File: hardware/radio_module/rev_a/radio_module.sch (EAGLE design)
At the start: 121 parts, among them J1 MODULE_GENERIC, J2 TC2030-JLINK-NL, J4 NANO_SIM, J5 TC2030-JLINK-L, P1 MOLEX_73251-135X, P2 MOLEX_73251-135X, Q1 MOSFET-NCHANNELXFDN-3, Q2 MOSFET-NCHANNELXFDN-3, Q3 MOSFET-NCHANNELXFDN-3, Q4 MOSFET-NCHANNELXFDN-3, Q5 NX3008PBK, Q6 NX3008PBK, Q7 NX3008PBK, U1 NUCLEUM, U10 TXB0106, U11 SAM4LC8BA, U12 UBLOX_SARA_G350, U2 TLV62130, U4 LTC2941, U5 LTC2941, U6 IM880_MODULE, U7 PCA9544AQFN-N20, U8 TLV62130, U9 LTC2941, X2 16 MHz

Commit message: used pats tool. worked well
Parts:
- removed C28, C32: 10uF, passives:CAPACITOR0402_CAP
- removed C30, C34: 3.3nF, passives:CAPACITOR0402_CAP
- removed C31, C35: 22uF, passives:CAPACITOR0402_CAP
- added C11: 10nF, passives:CAPACITOR0402_CAP
- added C14, C15, C16, C17, C18: 100nF, passives:CAPACITOR0402_CAP
- C1, C2: value 47pF -> 8pF; DIGIKEY (none) -> 490-8230-1-ND
- C10: value 56pF -> 3.3nF
- C19: value 1uF -> 100nF; DIGIKEY (none) -> 490-10777-1-ND
- C20: value 8 pF -> 100nF; DIGIKEY 490-8230-1-ND -> (none)
- C21: value 8 pF -> 1uF; DIGIKEY 490-8230-1-ND -> (none)
- C22: value 100 nF -> 4.7uF; DIGIKEY 490-10777-1-ND -> 490-13252-1-ND
- C23, C24: value 100 nF -> 10uF; DIGIKEY 490-10777-1-ND -> (none)
- C25, C26: value 100 nF -> 22uF; DIGIKEY 490-10777-1-ND -> (none)
- C27: value 4.7 uF -> 220uF; device passives:CAPACITOR0402_CAP -> passives:CAPACITOR1210_CAP; DIGIKEY 490-13252-1-ND -> (none)
- C3: value 47pF -> 33pF; device passives:CAPACITOR0402_CAP -> passives:CAPACITOR0603_CAP
- C5: value 33pF -> 47pF; device passives:CAPACITOR0603_CAP -> passives:CAPACITOR0402_CAP
- C6: value 100nF -> 47pF
- C7: value 220uF -> 47pF; device passives:CAPACITOR1210_CAP -> passives:CAPACITOR0402_CAP
- C8: value 100nF -> 56pF
- C9: value 10nF -> 3.3nF
- FB4: value 1.5 k -> 1.5k
- L6: value 22 uH -> 22uH
- R1: value 10K -> 0
- R10: value 1k -> 10k
- R11, R12: value 0 -> 10k; DIGIKEY (none) -> 1276-3431-1-ND
- R13: value 750k -> 10k; DIGIKEY (none) -> 1276-3431-1-ND
- R14: value 240k -> 10k; DIGIKEY (none) -> 1276-3431-1-ND
- R15, R21: value 100K -> 10k
- R16, R17: value 100 k -> 10k; DIGIKEY 1276-3432-1-ND -> (none)
- R18: value 10 k -> 10k; DIGIKEY 1276-3431-1-ND -> (none)
- R19: value 750k -> 10k
- R2: value 1k -> 0
- R20: value 200k -> 10k
- R24: DIGIKEY (none) -> 1276-3431-1-ND
- R25: value 0.423 -> 100k
- R26, R27: value 10k -> 100k; DIGIKEY (none) -> 1276-3432-1-ND
- R28, R30, R31, R32: value 10k -> 100k
- R29: value 0.016 -> 100k
- R3: value 100k -> 0; DIGIKEY (none) -> 1276-3431-1-ND
- R33: value 10k -> 100k; DIGIKEY 1276-3431-1-ND -> (none)
- R38: value 100k -> 200k
- R39: value 100k -> 240k
- R4: value 10k -> 0
- R40, R41: value 100k -> 750k
- R5: value 0 -> 0.016; DIGIKEY 1276-3431-1-ND -> (none)
- R6: value 0 -> 0.423; DIGIKEY 1276-3431-1-ND -> (none)
- R7: value 10k -> 3.333; DIGIKEY 1276-3431-1-ND -> (none)
- R8: value 10k -> 1k; DIGIKEY 1276-3431-1-ND -> (none)
- R9: value 3.333 -> 1k
- renumbered C29 to C12, C33 to C13
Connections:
- net 3V3: now also C16.1, C17.1, C18.1, C25.2, R11.2, R12.1, R13.1, R14.1, R19.2, R20.2, R24.1, R40.2, R6.2, R7.2; no longer C23.1, C24.1, C25.1, C31.2, R13.2, R22.2, R23.2, R24.2, R25.2, R33.1, R4.1, R7.1, R8.1, R9.2
- net 3V8: now also C26.2, R22.2, R23.2, R41.2, R5.2; no longer C35.2, R19.2, R30.2, R31.2, R32.2
- net 5V: now also C23.1, C24.1; no longer C28.1, C32.1
- net CONTROLLER_BUCK/LDO_N: now also R11.1; no longer R18.1
- net CONTROLLER_SWDCLK: now also R27.1; no longer R17.1
- net CONTROLLER_SWDIO: now also R26.1; no longer R16.1
- net CONTROLLER_XIN: now also C1.1; no longer C20.1
- net CONTROLLER_XOUT: now also C2.1; no longer C21.1
- net GND: now also C10.1, C11.2, C14.2, C15.2, C16.2, C17.2, C18.2, C25.1, C26.1, C5.2, C9.1, R30.1, R31.1, R32.1, R37.1, R38.1; no longer C10.2, C25.2, C26.2, C28.2, C3.2, C30.1, C31.1, C32.2, C34.1, C35.1, C9.2, R14.1, R20.1, R34.1, R36.1, R41.1
- net GSM_3V8: now also R33.2, R5.1, R8.2; no longer R2.2, R29.1, R37.2
- net GSM_GATED: now also C11.1, C14.1, C27.1; no longer C10.1, C7.1, C9.1
- net GSM_GAUGE_ALERT: now also R21.1; no longer R30.1
- net GSM_GAUGE_SCL: now also R22.1; no longer R31.1
- net GSM_GAUGE_SDA: now also R23.1; no longer R32.1
- net GSM_LED: now also R31.2; no longer R35.2
- net GSM_POWER_GATE: now also R32.2, R33.1; no longer R36.2, R37.1
- net IM880_3V3: now also R36.2, R6.1, R9.2; no longer R10.2, R25.1, R40.2
- net IM880_GATED: now also C21.1; no longer C19.1
- net IM880_GAUGE_ALERT: now also R18.1; no longer R26.1
- net IM880_GAUGE_SCL: now also R19.1; no longer R27.1
- net IM880_GAUGE_SDA: now also R20.1; no longer R28.1
- net IM880_NETWORK: now also R30.2; no longer R34.2
- net IM880_POWER_GATE: now also R36.1, R37.2; no longer R40.1, R41.2
- net N$1: now also C7.1; no longer C4.1
- net N$12: now also R24.2; no longer R33.2
- net N$15: now also C20.1, R25.2; no longer C6.1, R3.2
- net N$16: now also R25.1; no longer R3.1
- net N$17: now also R3.1; no longer R5.1
- net N$18: now also R4.1; no longer R6.1
- net N$2: now also C6.1; no longer C3.1
- net N$25: now also R1.1; no longer R11.1
- net N$26: now also R2.1; no longer R12.1
- net N$27: now also R9.1; no longer R10.1
- net N$3: now also C5.1; no longer C2.1
- net N$33: now also C15.1; no longer C22.1
- net N$34: now also C9.2; no longer C30.2
- net N$36: now also R28.1; no longer R15.1
- net N$37: now also R39.2, R40.1; no longer R13.1, R14.2
- net N$38: now also C10.2; no longer C34.2
- net N$4: now also C4.1; no longer C1.1
- net N$40: now also R29.1; no longer R21.1
- net N$41: now also R38.2, R41.1; no longer R19.1, R20.2
- net N$44: now also C19.1, C22.1; no longer C26.1, C27.1
- net N$5: now also R10.1; no longer R1.1
- net N$6: now also C3.1; no longer C5.1
- net N$7: now also C3.2; no longer C5.2
- net N$8: now also R8.1; no longer R2.1
- net N$9: now also R14.2; no longer R8.2
- net NUCLEUM_3V3: now also R34.2, R7.1; no longer R38.2, R9.1
- net NUCLEUM_GAUGE_ALERT: now also R15.1; no longer R22.1
- net NUCLEUM_GAUGE_SCL: now also R16.1; no longer R23.1
- net NUCLEUM_GAUGE_SDA: now also R17.1; no longer R24.1
- net NUCLEUM_POWER_GATE: now also R34.1, R35.2; no longer R38.1, R39.2
- net SCL: now also R2.2, R4.2; no longer R12.2, R6.2
- net SCL_INTERNAL: now also R13.2; no longer R7.2
- net SDA: now also R1.2, R3.2; no longer R11.2, R5.2
- net SDA_INTERNAL: now also R12.2; no longer R4.2
- net V_GSM_INT: now also R10.2; no longer R1.2
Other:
- moved on the sheet: C22, C3, C4, C5, C6, C7, C8, R15, R19, R20, R21, R22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

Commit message: also renumbered inductors after fixing script
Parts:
- removed L6: 22uH, signpost:LHQ3NP
- added L1: 2.2uH, passives:INDUCTORIHL
- L3: value 2.2uH -> 22uH; device passives:INDUCTORIHL -> signpost:LHQ3NP
- renumbered L4 to L2
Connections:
- net 3V3: now also L1.2; no longer L3.2
- net 3VSWOUT: now also L1.1; no longer L3.1
- net N$44: now also L3.1; no longer L6.1
- net N$52: now also L3.2; no longer L6.2
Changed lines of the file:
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@@
 <attribute name="DIGIKEY" value="490-5216-1-ND"/>
 </part>
-<part name="L6" library="signpost" deviceset="LHQ3NP" device="" value="22uH"/>
+<part name="L3" library="signpost" deviceset="LHQ3NP" device="" value="22uH"/>
 <part name="C19" library="passives" deviceset="CAPACITOR" device="0402_CAP" value="100nF">
 <attribute name="DIGIKEY" value="490-10777-1-ND"/>
@@
 <part name="R39" library="passives" deviceset="RESISTOR" device="0402_RES" value="240k"/>
 <part name="R28" library="passives" deviceset="RESISTOR" device="0402_RES" value="100k"/>
-<part name="L3" library="passives" deviceset="INDUCTOR" device="IHL" value="2.2uH"/>
+<part name="L1" library="passives" deviceset="INDUCTOR" device="IHL" value="2.2uH"/>
 <part name="U8" library="chips" deviceset="TLV62130" device=""/>
 <part name="C24" library="passives" deviceset="CAPACITOR" device="0402_CAP" value="10uF"/>
@@
 <part name="R38" library="passives" deviceset="RESISTOR" device="0402_RES" value="200k"/>
 <part name="R29" library="passives" deviceset="RESISTOR" device="0402_RES" value="100k"/>
-<part name="L4" library="passives" deviceset="INDUCTOR" device="IHL" value="2.2uH"/>
+<part name="L2" library="passives" deviceset="INDUCTOR" device="IHL" value="2.2uH"/>
 <part name="U11" library="chips" deviceset="SAM4LC8BA" device=""/>
 <part name="GND10" library="umich" deviceset="GND" device=""/>
@@
 <attribute name="DIGIKEY" x="91.44" y="154.94" size="1.27" layer="96" font="vector" rot="R90" display="off"/>
 </instance>
-<instance part="L6" gate="G$1" x="106.68" y="142.24" rot="R90"/>
+<instance part="L3" gate="G$1" x="106.68" y="142.24" rot="R90"/>
 <instance part="C19" gate="G$1" x="106.68" y="134.62">
 <attribute name="DIGIKEY" x="106.68" y="134.62" size="1.27" layer="96" align="bottom-center" display="off"/>
@@
 <net name="N$44" class="0">
 <segment>
-<pinref part="L6" gate="G$1" pin="1"/>
+<pinref part="L3" gate="G$1" pin="1"/>
 <wire x1="134.62" y1="134.62" x2="129.54" y2="134.62" width="0.1524" layer="91"/>
 <wire x1="129.54" y1="134.62" x2="129.54" y2="139.7" width="0.1524" layer="91"/>
@@
 <net name="N$52" class="0">
 <segment>
-<pinref part="L6" gate="G$1" pin="2"/>
+<pinref part="L3" gate="G$1" pin="2"/>
 <pinref part="U11" gate="G$1" pin="VDDCORE"/>
 <wire x1="114.3" y1="142.24" x2="132.08" y2="142.24" width="0.1524" layer="91"/>
@@
 <instance part="R39" gate="G$1" x="91.44" y="154.94" rot="R90"/>
 <instance part="R28" gate="G$1" x="83.82" y="167.64" rot="R90"/>
-<instance part="L3" gate="G$1" x="68.58" y="172.72" rot="R90"/>
+<instance part="L1" gate="G$1" x="68.58" y="172.72" rot="R90"/>
 <instance part="U8" gate="G$1" x="43.18" y="116.84"/>
 <instance part="C24" gate="G$1" x="7.62" y="121.92"/>
@@
 <instance part="R38" gate="G$1" x="91.44" y="109.22" rot="R90"/>
 <instance part="R29" gate="G$1" x="83.82" y="121.92" rot="R90"/>
-<instance part="L4" gate="G$1" x="68.58" y="127" rot="R90"/>
+<instance part="L2" gate="G$1" x="68.58" y="127" rot="R90"/>
 <instance part="U5" gate="G$1" x="144.78" y="147.32"/>
 <instance part="GND12" gate="1" x="160.02" y="132.08"/>
@@
 <segment>
 <pinref part="U2" gate="G$1" pin="SW"/>
-<pinref part="L3" gate="G$1" pin="1"/>
+<pinref part="L1" gate="G$1" pin="1"/>
 <wire x1="58.42" y1="172.72" x2="60.96" y2="172.72" width="0.1524" layer="91"/>
 </segment>
@@
 <wire x1="58.42" y1="167.64" x2="78.74" y2="167.64" width="0.1524" layer="91"/>
 <wire x1="78.74" y1="167.64" x2="78.74" y2="172.72" width="0.1524" layer="91"/>
-<pinref part="L3" gate="G$1" pin="2"/>
+<pinref part="L1" gate="G$1" pin="2"/>
 <wire x1="78.74" y1="172.72" x2="76.2" y2="172.72" width="0.1524" layer="91"/>
 <pinref part="R28" gate="G$1" pin="2"/>
@@
 <segment>
 <pinref part="U8" gate="G$1" pin="SW"/>
-<pinref part="L4" gate="G$1" pin="1"/>
+<pinref part="L2" gate="G$1" pin="1"/>
 <wire x1="58.42" y1="127" x2="60.96" y2="127" width="0.1524" layer="91"/>
 </segment>
@@
 <wire x1="58.42" y1="121.92" x2="78.74" y2="121.92" width="0.1524" layer="91"/>
 <wire x1="78.74" y1="121.92" x2="78.74" y2="127" width="0.1524" layer="91"/>
-<pinref part="L4" gate="G$1" pin="2"/>
+<pinref part="L2" gate="G$1" pin="2"/>
 <wire x1="78.74" y1="127" x2="76.2" y2="127" width="0.1524" layer="91"/>
 <pinref part="R29" gate="G$1" pin="2"/>

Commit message: updated a few packages, made traces wider
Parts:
- R5: value 0.016 -> 0.015; device passives:RESISTOR0402_RES -> passives:RESISTOR0603_RES
- R6: value 0.423 -> 0.43
- R7: value 3.333 -> 3.32
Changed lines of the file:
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@@
 <schematic xreflabel="%F%N/%S" xrefpart="/%S">
 <attributes>
+<attribute name="AUTHOR" value="Joshua Adkins"/>
+<attribute name="REV" value="A"/>
+<attribute name="TITLE" value="Radio Module"/>
 </attributes>
 <variantdefs>
@@
 <part name="GND11" library="umich" deviceset="GND" device=""/>
 <part name="GND12" library="umich" deviceset="GND" device=""/>
-<part name="R7" library="passives" deviceset="RESISTOR" device="0402_RES" value="3.333"/>
+<part name="R7" library="passives" deviceset="RESISTOR" device="0402_RES" value="3.32"/>
 <part name="R15" library="passives" deviceset="RESISTOR" device="0402_RES" value="10k"/>
 <part name="R16" library="passives" deviceset="RESISTOR" device="0402_RES" value="10k"/>
@@
 <part name="U4" library="signpost" deviceset="LTC2941" device=""/>
 <part name="GND13" library="umich" deviceset="GND" device=""/>
-<part name="R6" library="passives" deviceset="RESISTOR" device="0402_RES" value="0.423"/>
+<part name="R6" library="passives" deviceset="RESISTOR" device="0402_RES" value="0.43"/>
 <part name="R18" library="passives" deviceset="RESISTOR" device="0402_RES" value="10k"/>
 <part name="R19" library="passives" deviceset="RESISTOR" device="0402_RES" value="10k"/>
@@
 <part name="U9" library="signpost" deviceset="LTC2941" device=""/>
 <part name="GND24" library="umich" deviceset="GND" device=""/>
-<part name="R5" library="passives" deviceset="RESISTOR" device="0402_RES" value="0.016"/>
+<part name="R5" library="passives" deviceset="RESISTOR" device="0603_RES" value="0.015"/>
 <part name="R21" library="passives" deviceset="RESISTOR" device="0402_RES" value="10k"/>
 <part name="R22" library="passives" deviceset="RESISTOR" device="0402_RES" value="10k"/>

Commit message: finalized board and schematic
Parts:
- Q5, Q6, Q7: value NX3008PBK -> SI223DDS; device fets:NX3008PBK -> fets:SI223DDS
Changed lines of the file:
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@@
 <part name="R30" library="passives" deviceset="RESISTOR" device="0402_RES" value="100k"/>
 <part name="R31" library="passives" deviceset="RESISTOR" device="0402_RES" value="100k"/>
-<part name="Q5" library="fets" deviceset="NX3008PBK" device=""/>
+<part name="Q5" library="fets" deviceset="SI223DDS" device=""/>
 <part name="GND25" library="umich" deviceset="GND" device=""/>
 <part name="R32" library="passives" deviceset="RESISTOR" device="0402_RES" value="100k"/>
 <part name="R33" library="passives" deviceset="RESISTOR" device="0402_RES" value="100k"/>
-<part name="Q6" library="fets" deviceset="NX3008PBK" device=""/>
+<part name="Q6" library="fets" deviceset="SI223DDS" device=""/>
 <part name="R34" library="passives" deviceset="RESISTOR" device="0402_RES" value="100k"/>
 <part name="R35" library="passives" deviceset="RESISTOR" device="0402_RES" value="100k"/>
 <part name="GND26" library="umich" deviceset="GND" device=""/>
-<part name="Q7" library="fets" deviceset="NX3008PBK" device=""/>
+<part name="Q7" library="fets" deviceset="SI223DDS" device=""/>
 <part name="R36" library="passives" deviceset="RESISTOR" device="0402_RES" value="100k"/>
 <part name="R37" library="passives" deviceset="RESISTOR" device="0402_RES" value="100k"/>

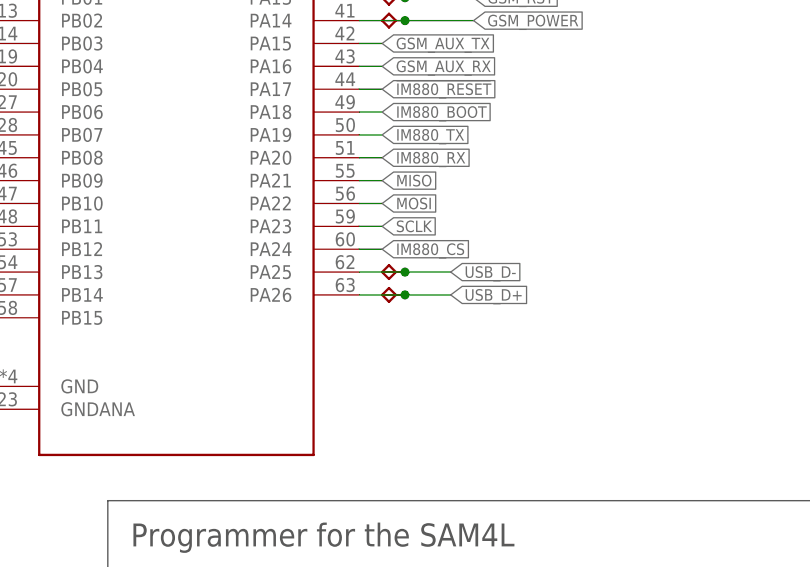
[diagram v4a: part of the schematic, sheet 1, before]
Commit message: more changes. Removed gerbers. Removed usb tps
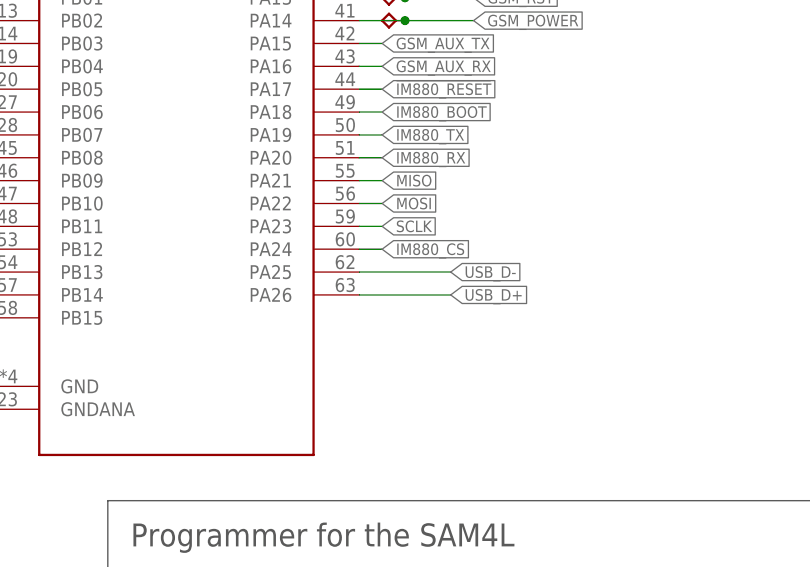
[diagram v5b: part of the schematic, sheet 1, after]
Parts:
- removed TP4, TP5: TPB1,27, testpad:TPB1,27
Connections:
- net USB_D+: no longer TP4.TP
- net USB_D-: no longer TP5.TP
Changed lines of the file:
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@@
 <part name="TP2" library="testpad" deviceset="TP" device="B1,27"/>
 <part name="TP3" library="testpad" deviceset="TP" device="B1,27"/>
-<part name="TP4" library="testpad" deviceset="TP" device="B1,27"/>
-<part name="TP5" library="testpad" deviceset="TP" device="B1,27"/>
 <part name="TP6" library="testpad" deviceset="TP" device="B1,27"/>
 <part name="TP7" library="testpad" deviceset="TP" device="B1,27"/>
@@
 <attribute name="TP_SIGNAL_NAME" x="130.81" y="118.11" size="1.778" layer="97" rot="R90"/>
 </instance>
-<instance part="TP4" gate="G$1" x="177.8" y="93.98" smashed="yes" rot="R90">
-<attribute name="TP_SIGNAL_NAME" x="179.07" y="95.25" size="1.778" layer="97" rot="R90"/>
-</instance>
-<instance part="TP5" gate="G$1" x="177.8" y="96.52" smashed="yes" rot="R90">
-<attribute name="TP_SIGNAL_NAME" x="179.07" y="97.79" size="1.778" layer="97" rot="R90"/>
-</instance>
 <instance part="TP6" gate="G$1" x="177.8" y="124.46" smashed="yes" rot="R90">
 <attribute name="TP_SIGNAL_NAME" x="179.07" y="125.73" size="1.778" layer="97" rot="R90"/>
@@
 <segment>
 <pinref part="U11" gate="G$1" pin="PA25"/>
-<wire x1="175.26" y1="96.52" x2="180.34" y2="96.52" width="0.1524" layer="91"/>
 <label x="185.42" y="96.52" size="1.27" layer="95" xref="yes"/>
-<pinref part="TP5" gate="G$1" pin="TP"/>
-<wire x1="180.34" y1="96.52" x2="185.42" y2="96.52" width="0.1524" layer="91"/>
-<junction x="180.34" y="96.52"/>
+<wire x1="175.26" y1="96.52" x2="185.42" y2="96.52" width="0.1524" layer="91"/>
 </segment>
 <segment>
@@
 <segment>
 <pinref part="U11" gate="G$1" pin="PA26"/>
-<wire x1="175.26" y1="93.98" x2="180.34" y2="93.98" width="0.1524" layer="91"/>
 <label x="185.42" y="93.98" size="1.27" layer="95" xref="yes"/>
-<pinref part="TP4" gate="G$1" pin="TP"/>
-<wire x1="180.34" y1="93.98" x2="185.42" y2="93.98" width="0.1524" layer="91"/>
-<junction x="180.34" y="93.98"/>
-</segment>
-<segment>
+<wire x1="175.26" y1="93.98" x2="185.42" y2="93.98" width="0.1524" layer="91"/>
+</segment>
+<segment>

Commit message: added better rf traces, made the board four layers
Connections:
- removed net N$29: P2.P$2, U6.RF
- new net N$24: P2.ANT, U6.RF
- net GND: now also P1.P$2, P2.P$2
- net N$7: now also P1.ANT; no longer P1.P$2
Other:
- moved on the sheet: P2
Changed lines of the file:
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@@
 <part name="TP17" library="testpad" deviceset="PTR1" device="PAD1-13" value="PTR1PAD1-13"/>
 <part name="U$1" library="logos" deviceset="UCB_CAL" device="100MIL"/>
+<part name="GND29" library="umich" deviceset="GND" device=""/>
+<part name="GND30" library="umich" deviceset="GND" device=""/>
 </parts>
 <sheets>
@@
 <instance part="C20" gate="G$1" x="99.06" y="132.08"/>
 <instance part="U10" gate="G$1" x="40.64" y="96.52" rot="MR0"/>
+<instance part="GND29" gate="1" x="210.82" y="96.52"/>
 </instances>
 <busses>
@@
 <wire x1="172.72" y1="147.32" x2="172.72" y2="144.78" width="0.1524" layer="91"/>
 </segment>
+<segment>
+<pinref part="P1" gate="G$1" pin="P$2"/>
+<pinref part="GND29" gate="1" pin="GND"/>
+<wire x1="210.82" y1="101.6" x2="210.82" y2="99.06" width="0.1524" layer="91"/>
+</segment>
 </net>
 <net name="N$4" class="0">
@@
 <pinref part="C3" gate="G$1" pin="1"/>
 <wire x1="175.26" y1="99.06" x2="187.96" y2="99.06" width="0.1524" layer="91"/>
-</segment>
-</net>
-<net name="N$7" class="0">
-<segment>
-<pinref part="C3" gate="G$1" pin="2"/>
-<wire x1="195.58" y1="99.06" x2="210.82" y2="99.06" width="0.1524" layer="91"/>
-<wire x1="210.82" y1="99.06" x2="210.82" y2="101.6" width="0.1524" layer="91"/>
-<pinref part="P1" gate="G$1" pin="P$2"/>
 </segment>
 </net>
@@
 <label x="20.32" y="96.52" size="1.27" layer="95" rot="R180" xref="yes"/>
 <pinref part="U10" gate="G$1" pin="B2"/>
+</segment>
+</net>
+<net name="N$7" class="0">
+<segment>
+<pinref part="C3" gate="G$1" pin="2"/>
+<wire x1="195.58" y1="99.06" x2="203.2" y2="99.06" width="0.1524" layer="91"/>
+<wire x1="203.2" y1="99.06" x2="203.2" y2="106.68" width="0.1524" layer="91"/>
+<pinref part="P1" gate="G$1" pin="ANT"/>
+<wire x1="203.2" y1="106.68" x2="208.28" y2="106.68" width="0.1524" layer="91"/>
 </segment>
 </net>
@@
 </instance>
 <instance part="GND17" gate="1" x="83.82" y="71.12"/>
-<instance part="P2" gate="G$1" x="195.58" y="114.3"/>
+<instance part="P2" gate="G$1" x="195.58" y="109.22"/>
 <instance part="J2" gate="G$1" x="27.94" y="152.4"/>
 <instance part="R1" gate="G$1" x="215.9" y="93.98" smashed="yes">
@@
 <instance part="R37" gate="G$1" x="142.24" y="129.54" rot="R90"/>
 <instance part="GND28" gate="1" x="142.24" y="119.38"/>
+<instance part="GND30" gate="1" x="195.58" y="99.06"/>
 </instances>
 <busses>
@@
 <wire x1="142.24" y1="121.92" x2="142.24" y2="124.46" width="0.1524" layer="91"/>
 </segment>
+<segment>
+<pinref part="GND30" gate="1" pin="GND"/>
+<pinref part="P2" gate="G$1" pin="P$2"/>
+<wire x1="195.58" y1="101.6" x2="195.58" y2="104.14" width="0.1524" layer="91"/>
+</segment>
 </net>
 <net name="MISO" class="0">
@@
 <pinref part="LED2" gate="G$1" pin="CATHODE"/>
 <wire x1="83.82" y1="93.98" x2="83.82" y2="96.52" width="0.1524" layer="91"/>
-</segment>
-</net>
-<net name="N$29" class="0">
-<segment>
-<pinref part="U6" gate="G$1" pin="RF"/>
-<pinref part="P2" gate="G$1" pin="P$2"/>
-<wire x1="182.88" y1="109.22" x2="195.58" y2="109.22" width="0.1524" layer="91"/>
 </segment>
 </net>
@@
 </segment>
 </net>
+<net name="N$24" class="0">
+<segment>
+<pinref part="U6" gate="G$1" pin="RF"/>
+<pinref part="P2" gate="G$1" pin="ANT"/>
+<wire x1="182.88" y1="109.22" x2="193.04" y2="109.22" width="0.1524" layer="91"/>
+</segment>
+</net>
